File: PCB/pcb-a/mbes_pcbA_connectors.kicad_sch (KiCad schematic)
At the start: 17 parts, among them U3 L7805

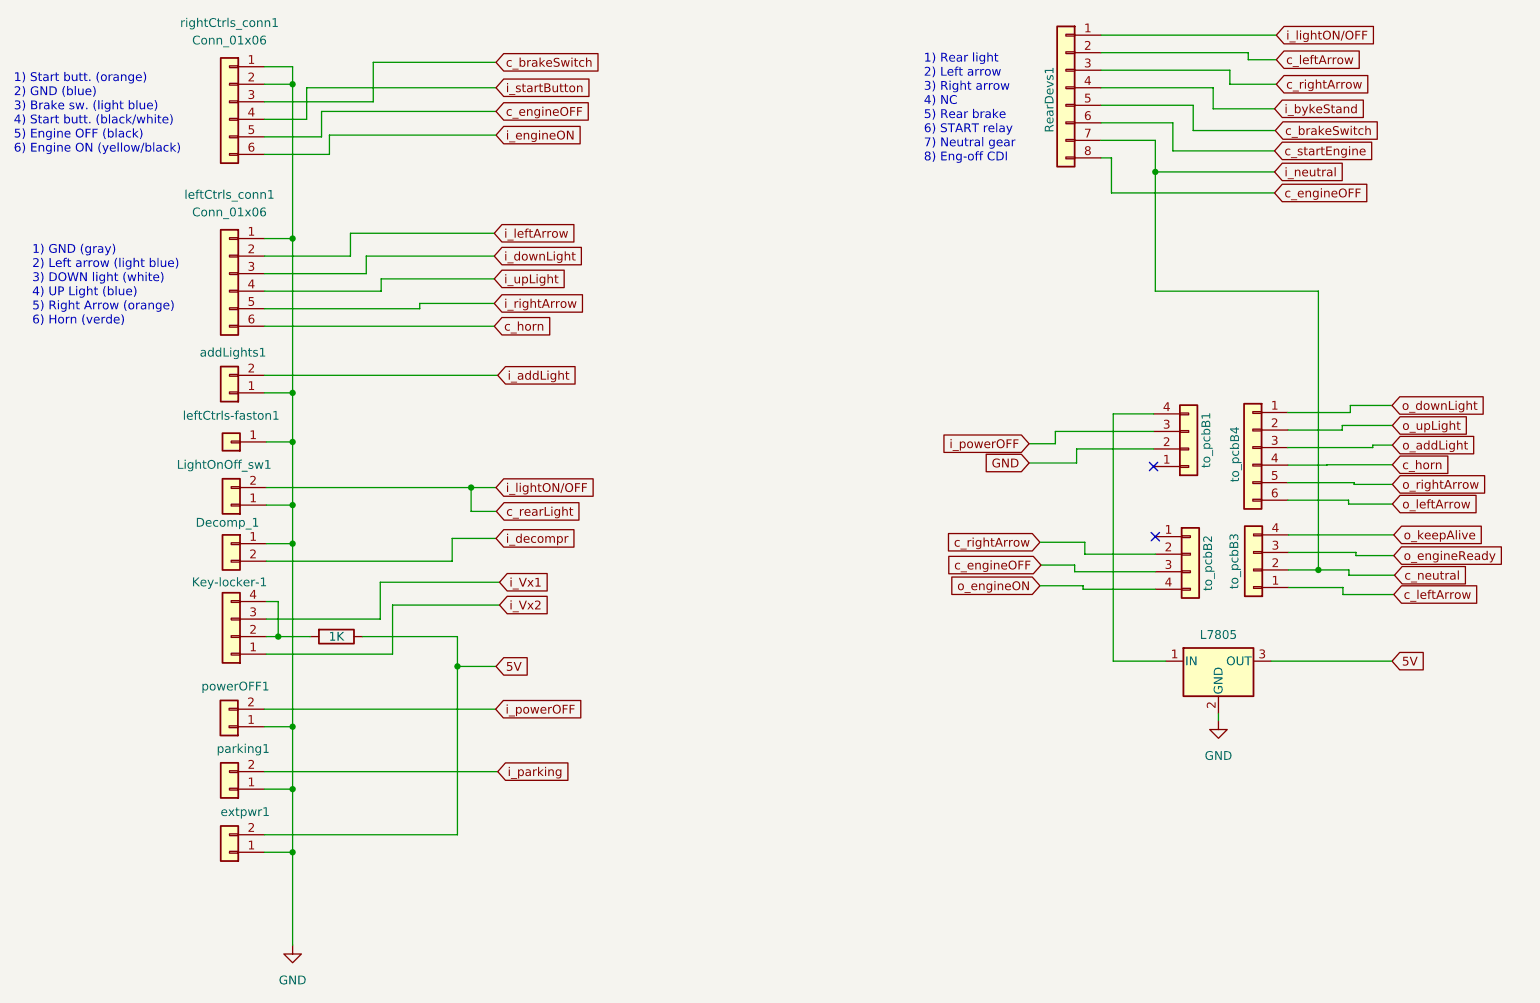
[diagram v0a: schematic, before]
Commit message: Update for connectors change
The four connectors that linked pcb-a with pcb-b have been replaced with two dual line connectors.
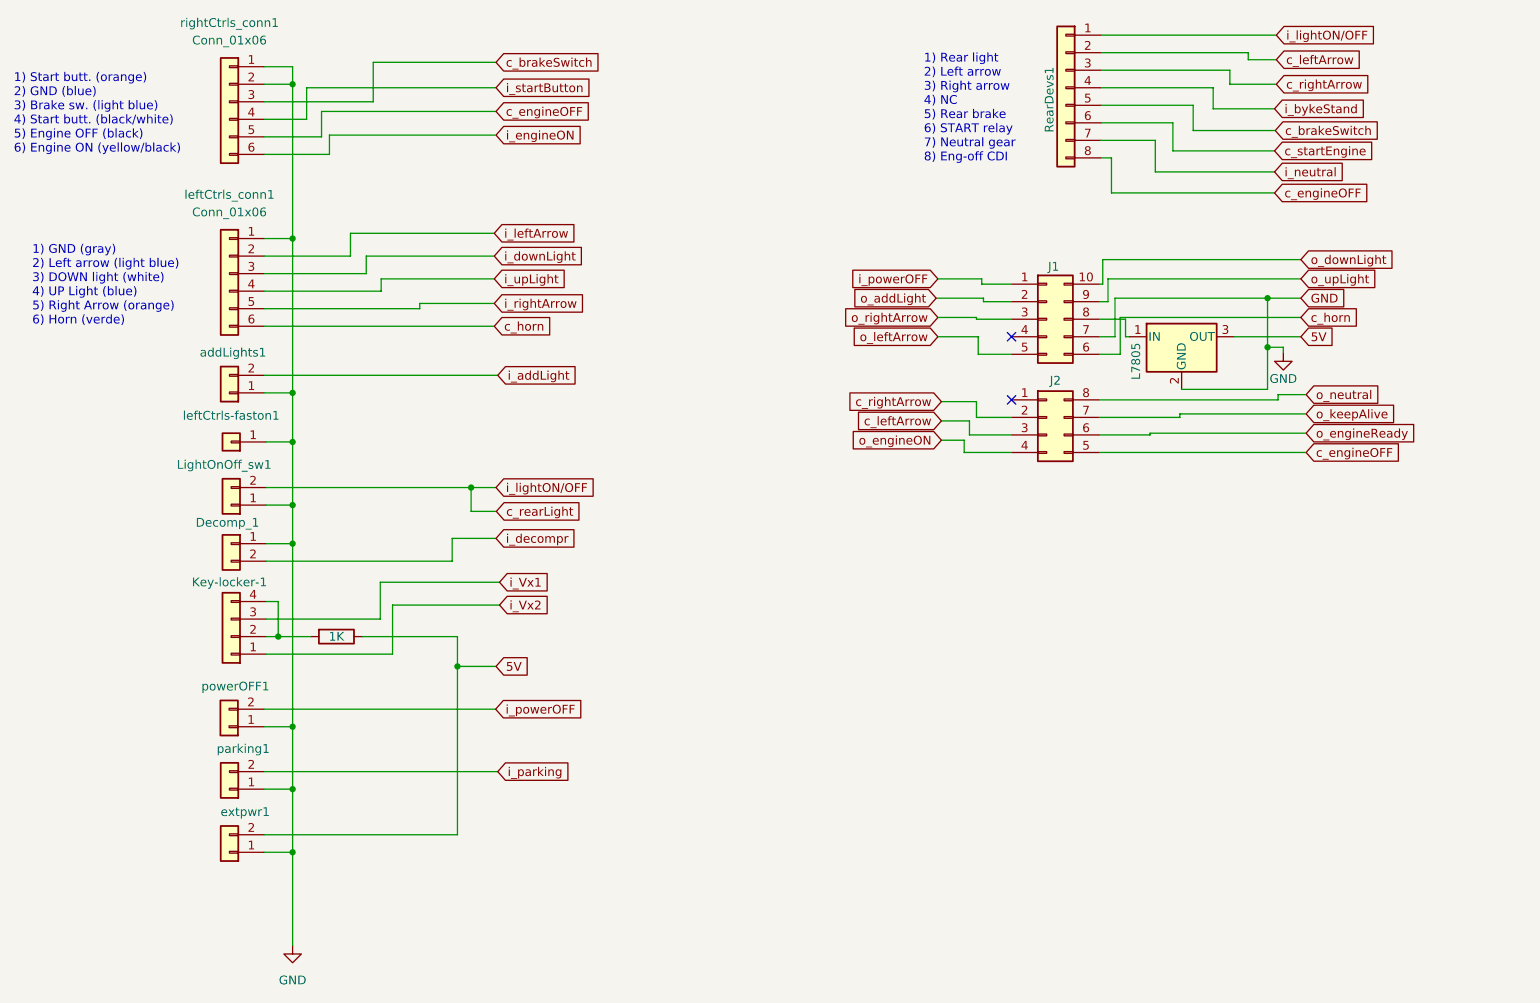
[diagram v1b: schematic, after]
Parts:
- removed to_pcbB1, to_pcbB2, to_pcbB3: Conn_01x04, Connector_PinHeader_2.54mm:PinHeader_1x04_P2.54mm_Vertical, symbol Connector_Generic:Conn_01x04
- removed to_pcbB4: Conn_01x06, Connector_PinHeader_2.54mm:PinHeader_1x06_P2.54mm_Vertical, symbol Connector_Generic:Conn_01x06
- added J1: Conn_02x05_Counter_Clockwise, symbol Connector_Generic:Conn_02x05_Counter_Clockwise
- added J2: Conn_02x04_Counter_Clockwise, symbol Connector_Generic:Conn_02x04_Counter_Clockwise
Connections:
- net GND: now also J1.7 (Pin_7)
- net c_engineOFF: now also J2.5 (Pin_5)
- net c_horn: now also J1.6 (Pin_6)
- net c_leftArrow: now also J2.3 (Pin_3)
- net c_rightArrow: now also J2.2 (Pin_2)
- net i_powerOFF: now also J1.1 (Pin_1)
- net o_addLight: now also J1.2 (Pin_2)
- net o_downLight: now also J1.10 (Pin_10)
- net o_engineON: now also J2.4 (Pin_4)
- net o_engineReady: now also J2.6 (Pin_6)
- net o_keepAlive: now also J2.7 (Pin_7)
- net o_leftArrow: now also J1.5 (Pin_5)
- net o_rightArrow: now also J1.3 (Pin_3)
- net o_upLight: now also J1.9 (Pin_9)
- net at U3.1 (IN): now also J1.8 (Pin_8)
- net c_neutral renamed i_neutral
- new net o_neutral: J2.8 (Pin_8)

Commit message: Fixes and updates
This version will be tested soon. It is fully implemented with THT devices using ESP32-S2 DevKit
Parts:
- removed parking1: Conn_01x02, Connector_Wire:SolderWire-0.15sqmm_1x02_P4mm_D0.5mm_OD1.5mm, symbol Connector_Generic:Conn_01x02
- J1: footprint (none) -> Connector_PinHeader_2.54mm:PinHeader_2x05_P2.54mm_Vertical
- J2: footprint (none) -> Connector_PinHeader_2.54mm:PinHeader_2x04_P2.54mm_Vertical
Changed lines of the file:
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@@
 	)
 	(junction
-		(at 65.786 157.988)
-		(diameter 0)
-		(color 0 0 0 0)
-	)
-	(junction
 		(at 63.7032 135.89)
 		(diameter 0)
@@
 	(wire
 		(pts
-			(xy 61.722 155.448) (xy 95.504 155.448)
-		)
-		(stroke
-			(width 0)
-			(type default)
-		)
-	)
-	(wire
-		(pts
 			(xy 208.1276 62.5856) (xy 196.2404 62.5856)
 		)
@@
 	(wire
 		(pts
-			(xy 61.722 157.988) (xy 65.786 157.988)
-		)
-		(stroke
-			(width 0)
-			(type default)
-		)
-	)
-	(wire
-		(pts
 			(xy 182.88 58.928) (xy 196.2404 58.928)
 		)
@@
 	(wire
 		(pts
-			(xy 65.786 157.988) (xy 65.786 148.9456)
-		)
-		(stroke
-			(width 0)
-			(type default)
-		)
-	)
-	(wire
-		(pts
 			(xy 201.549 53.848) (xy 201.549 55.88)
 		)
@@
 	(wire
 		(pts
-			(xy 65.786 167.132) (xy 65.786 157.988)
+			(xy 65.786 148.9456) (xy 65.786 167.132)
 		)
 		(stroke
@@
 		)
 	)
-	(global_label "i_parking"
-		(shape input)
-		(at 95.504 155.448 0)
-		(fields_autoplaced yes)
-		(effects
-			(font
-				(size 1.27 1.27)
-			)
-			(justify left)
-		)
-		(property "Intersheetrefs" "${INTERSHEET_REFS}"
-			(at 107.0767 155.448 0)
-			(effects
-				(font
-					(size 1.27 1.27)
-				)
-				(justify left)
-				(hide yes)
-			)
-		)
-		(property "Riferimenti inter-foglio" "${INTERSHEET_REFS}"
-			(at 95.504 157.6388 0)
-			(effects
-				(font
-					(size 1.27 1.27)
-				)
-				(justify left)
-				(hide yes)
-			)
-		)
-	)
 	(global_label "c_rearLight"
 		(shape input)
@@
 			)
 		)
-		(property "Footprint" ""
+		(property "Footprint" "Connector_PinHeader_2.54mm:PinHeader_2x04_P2.54mm_Vertical"
 			(at 175.006 104.14 0)
 			(effects
@@
 	)
 	(symbol
-		(lib_id "Connector_Generic:Conn_01x02")
-		(at 56.642 157.988 180)
-		(unit 1)
-		(exclude_from_sim no)
-		(in_bom yes)
-		(on_board yes)
-		(dnp no)
-		(property "Reference" "parking1"
-			(at 62.484 152.146 0)
-			(effects
-				(font
-					(size 1.27 1.27)
-				)
-				(justify left)
-			)
-		)
-		(property "Value" "Conn_01x02"
-			(at 55.3721 160.528 90)
-			(effects
-				(font
-					(size 1.27 1.27)
-				)
-				(justify left)
-				(hide yes)
-			)
-		)
-		(property "Footprint" "Connector_Wire:SolderWire-0.15sqmm_1x02_P4mm_D0.5mm_OD1.5mm"
-			(at 56.642 157.988 0)
-			(effects
-				(font
-					(size 1.27 1.27)
-				)
-				(hide yes)
-			)
-		)
-		(property "Datasheet" "~"
-			(at 56.642 157.988 0)
-			(effects
-				(font
-					(size 1.27 1.27)
-				)
-				(hide yes)
-			)
-		)
-		(property "Description" ""
-			(at 56.642 157.988 0)
-			(effects
-				(font
-					(size 1.27 1.27)
-				)
-				(hide yes)
-			)
-		)
-		(pin "1"
-		)
-		(pin "2"
-		)
-		(instances
-			(project "pcb-a"
-				(path "/709d0967-afe5-49d3-92a5-d2bb94550bdb/3216a3d3-5416-4017-b51b-dad2d5be039c"
-					(reference "parking1")
-					(unit 1)
-				)
-			)
-		)
-	)
-	(symbol
 		(lib_id "Device:R")
 		(at 72.136 135.89 270)
@@
 			)
 		)
-		(property "Footprint" ""
+		(property "Footprint" "Connector_PinHeader_2.54mm:PinHeader_2x05_P2.54mm_Vertical"
 			(at 175.006 89.916 0)
 			(effects

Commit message: Changes to reduce PCB size
- The resistors type has been changed from THT to SMD
- Configuration switches has been moved to fit PCB space in better way
- An electrolitic capicitor has been added
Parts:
- R1: footprint Resistor_THT:R_Axial_DIN0204_L3.6mm_D1.6mm_P5.08mm_Horizontal -> Resistor_SMD:R_1206_3216Metric
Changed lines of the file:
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@@
 			)
 		)
-		(property "Footprint" "Resistor_THT:R_Axial_DIN0204_L3.6mm_D1.6mm_P5.08mm_Horizontal"
+		(property "Footprint" "Resistor_SMD:R_1206_3216Metric"
 			(at 72.136 134.112 90)
 			(effects
